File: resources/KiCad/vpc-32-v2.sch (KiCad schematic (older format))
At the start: 58 parts, among them CON1 Power jack, J1 SD_SOCKET, J2 PS/2, J3 video out, J4 RJ11, J5 audio out, K1 jumper, P1 gamepad 2, P2 ICSP, P3 gempad 1, Q1 2N3906, Q2 2N3904, SW1 reset, SW2 Power, U1 LM3940-3.3, U2 PIC32MX170F256B, U3 23LC1024, X1 10Mhz

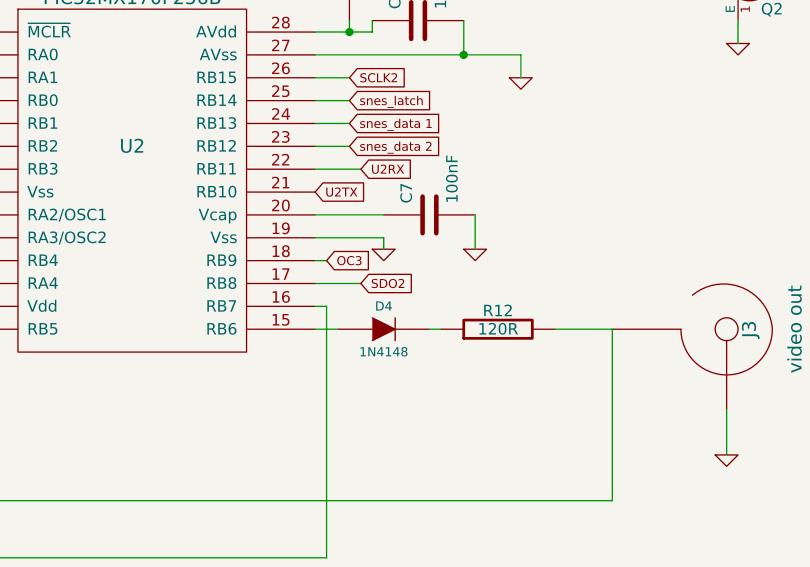
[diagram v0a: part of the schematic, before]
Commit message: ajout support sram et correction bug
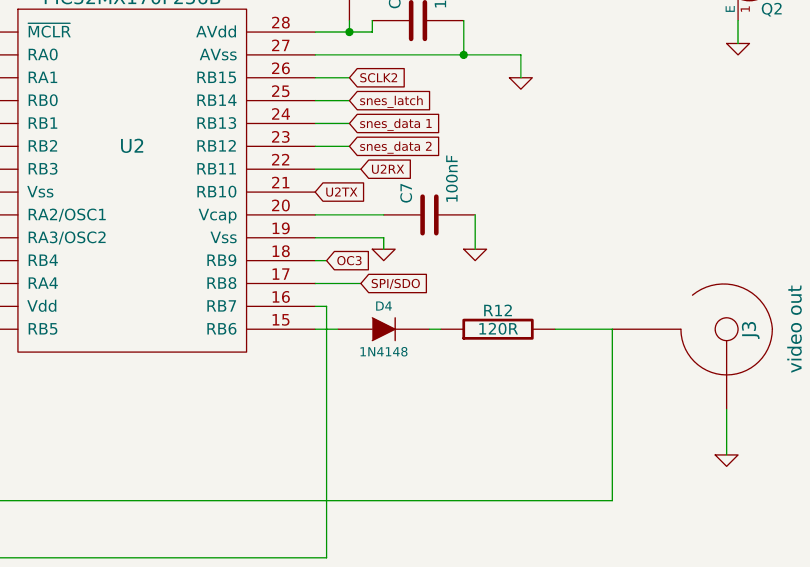
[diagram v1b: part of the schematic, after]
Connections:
- net SDO2 renamed SPI/SDO
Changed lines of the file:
@@
 Sheet 1 1
 Title ""
-Date "17 nov 2014"
+Date "24 nov 2014"
 Rev ""
 Comp ""
@@
 STATUS
 Text GLabel 6900 4150 2    39   Input ~ 0
-SDO2
+SPI/SDO
 Text GLabel 5000 3350 0    39   Input ~ 0
 PGED1/snes_clock

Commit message: travail sur vpcBASIC
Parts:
- added C14: 10µF, ~, symbol C
- added C15: 47µF, ~, symbol C
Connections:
- net +3,3V: now also C14.1, C15.1
- net GND: now also C14.2, C15.2
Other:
- note added: "+\n"
- note added: "C14 ceramic, SMD\nC1,C15 aluminum electrolytic through hole"
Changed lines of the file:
@@
 Sheet 1 1
 Title ""
-Date "24 nov 2014"
+Date "30 nov 2014"
 Rev ""
 Comp ""
@@
 $EndComp
 $Comp
-L GND #PWR21
+L GND #PWR23
 U 1 1 52181145
 P 8500 4900
-F 0 "#PWR21" H 8500 4900 30  0001 C CNN
+F 0 "#PWR23" H 8500 4900 30  0001 C CNN
 F 1 "GND" H 8500 4830 30  0001 C CNN
 F 2 "" H 8500 4900 60  0000 C CNN
@@
 +3,3V
 $Comp
-L GND #PWR16
+L GND #PWR18
 U 1 1 521812CB
 P 7000 4000
-F 0 "#PWR16" H 7000 4000 30  0001 C CNN
+F 0 "#PWR18" H 7000 4000 30  0001 C CNN
 F 1 "GND" H 7000 3930 30  0001 C CNN
 F 2 "" H 7000 4000 60  0000 C CNN
@@
 $EndComp
 $Comp
-L GND #PWR13
+L GND #PWR14
 U 1 1 521812EF
 P 4850 3750
-F 0 "#PWR13" H 4850 3750 30  0001 C CNN
+F 0 "#PWR14" H 4850 3750 30  0001 C CNN
 F 1 "GND" H 4850 3680 30  0001 C CNN
 F 2 "" H 4850 3750 60  0000 C CNN
@@
 $EndComp
 $Comp
-L GND #PWR17
+L GND #PWR19
 U 1 1 521A0F8C
 P 7400 4000
-F 0 "#PWR17" H 7400 4000 30  0001 C CNN
+F 0 "#PWR19" H 7400 4000 30  0001 C CNN
 F 1 "GND" H 7400 3930 30  0001 C CNN
 F 2 "" H 7400 4000 60  0000 C CNN
@@
 $EndComp
 $Comp
-L GND #PWR12
+L GND #PWR13
 U 1 1 521A10AE
 P 4600 2450
-F 0 "#PWR12" H 4600 2450 30  0001 C CNN
+F 0 "#PWR13" H 4600 2450 30  0001 C CNN
 F 1 "GND" H 4600 2380 30  0001 C CNN
 F 2 "" H 4600 2450 60  0000 C CNN
@@
 +3,3V
 $Comp
-L GND #PWR15
+L GND #PWR17
 U 1 1 521A28F4
 P 6000 1650
-F 0 "#PWR15" H 6000 1650 30  0001 C CNN
+F 0 "#PWR17" H 6000 1650 30  0001 C CNN
 F 1 "GND" H 6000 1580 30  0001 C CNN
 F 2 "" H 6000 1650 60  0000 C CNN
@@
 PGEC1
 $Comp
-L GND #PWR25
+L GND #PWR27
 U 1 1 521A78A1
 P 9750 2600
-F 0 "#PWR25" H 9750 2600 30  0001 C CNN
+F 0 "#PWR27" H 9750 2600 30  0001 C CNN
 F 1 "GND" H 9750 2530 30  0001 C CNN
 F 2 "" H 9750 2600 60  0000 C CNN
@@
 $EndComp
 $Comp
-L GND #PWR22
+L GND #PWR24
 U 1 1 521A7A94
 P 8550 3100
-F 0 "#PWR22" H 8550 3100 30  0001 C CNN
+F 0 "#PWR24" H 8550 3100 30  0001 C CNN
 F 1 "GND" H 8550 3030 30  0001 C CNN
 F 2 "" H 8550 3100 60  0000 C CNN
@@
 $EndComp
 $Comp
-L GND #PWR24
+L GND #PWR26
 U 1 1 521A7A9A
 P 9550 2950
-F 0 "#PWR24" H 9550 2950 30  0001 C CNN
+F 0 "#PWR26" H 9550 2950 30  0001 C CNN
 F 1 "GND" H 9550 2880 30  0001 C CNN
 F 2 "" H 9550 2950 60  0000 C CNN
@@
 $EndComp
 $Comp
-L GND #PWR19
+L GND #PWR21
 U 1 1 521A7BF6
 P 8150 2850
-F 0 "#PWR19" H 8150 2850 30  0001 C CNN
+F 0 "#PWR21" H 8150 2850 30  0001 C CNN
 F 1 "GND" H 8150 2780 30  0001 C CNN
 F 2 "" H 8150 2850 60  0000 C CNN
@@
 $EndComp
 $Comp
-L GND #PWR29
+L GND #PWR31
 U 1 1 521A9812
 P 10500 6350
-F 0 "#PWR29" H 10500 6350 30  0001 C CNN
+F 0 "#PWR31" H 10500 6350 30  0001 C CNN
 F 1 "GND" H 10500 6280 30  0001 C CNN
 F 2 "" H 10500 6350 60  0000 C CNN
@@
 $EndComp
 $Comp
-L GND #PWR26
+L GND #PWR28
 U 1 1 521A9A38
 P 9750 6450
-F 0 "#PWR26" H 9750 6450 30  0001 C CNN
+F 0 "#PWR28" H 9750 6450 30  0001 C CNN
 F 1 "GND" H 9750 6380 30  0001 C CNN
 F 2 "" H 9750 6450 60  0000 C CNN
@@
 $EndComp
 $Comp
-L GND #PWR23
+L GND #PWR25
 U 1 1 521A9A3E
 P 9250 6450
-F 0 "#PWR23" H 9250 6450 30  0001 C CNN
+F 0 "#PWR25" H 9250 6450 30  0001 C CNN
 F 1 "GND" H 9250 6380 30  0001 C CNN
 F 2 "" H 9250 6450 60  0000 C CNN
@@
 $EndComp
 $Comp
-L GND #PWR20
+L GND #PWR22
 U 1 1 521A9A4E
 P 8450 6450
-F 0 "#PWR20" H 8450 6450 30  0001 C CNN
+F 0 "#PWR22" H 8450 6450 30  0001 C CNN
 F 1 "GND" H 8450 6380 30  0001 C CNN
 F 2 "" H 8450 6450 60  0000 C CNN
@@
 $EndComp
 $Comp
-L GND #PWR14
+L GND #PWR16
 U 1 1 521E10D5
 P 5600 7200
-F 0 "#PWR14" H 5600 7200 30  0001 C CNN
+F 0 "#PWR16" H 5600 7200 30  0001 C CNN
 F 1 "GND" H 5600 7130 30  0001 C CNN
 F 2 "" H 5600 7200 60  0000 C CNN
@@
 PGEC1/~CS1
 $Comp
-L GND #PWR18
+L GND #PWR20
 U 1 1 5225165F
 P 7600 3250
-F 0 "#PWR18" H 7600 3250 30  0001 C CNN
+F 0 "#PWR20" H 7600 3250 30  0001 C CNN
 F 1 "GND" H 7600 3180 30  0001 C CNN
 F 2 "" H 7600 3250 60  0000 C CNN
@@
 $EndComp
 $Comp
-L GND #PWR28
+L GND #PWR30
 U 1 1 538B65CC
 P 10150 4900
-F 0 "#PWR28" H 10150 4900 30  0001 C CNN
+F 0 "#PWR30" H 10150 4900 30  0001 C CNN
 F 1 "GND" H 10150 4830 30  0001 C CNN
 F 2 "" H 10150 4900 60  0000 C CNN
@@
 $EndComp
 $Comp
-L GND #PWR27
+L GND #PWR29
 U 1 1 538B65D2
 P 10150 4000
-F 0 "#PWR27" H 10150 4000 30  0001 C CNN
+F 0 "#PWR29" H 10150 4000 30  0001 C CNN
 F 1 "GND" H 10150 3930 30  0001 C CNN
 F 2 "" H 10150 4000 60  0000 C CNN
@@
 Connection ~ 2900 5750
 Connection ~ 1650 6050
+$Comp
+L C C15
+U 1 1 547B4E3E
+P 4850 6900
+F 0 "C15" H 4850 7000 40  0000 L CNN
+F 1 "47µF" H 4856 6815 40  0000 L CNN
+F 2 "~" H 4888 6750 30  0000 C CNN
+F 3 "~" H 4850 6900 60  0000 C CNN
+	1    4850 6900
+	1    0    0    -1
+$EndComp
+$Comp
+L C C14
+U 1 1 547B4E4B
+P 4450 6900
+F 0 "C14" H 4450 7000 40  0000 L CNN
+F 1 "10µF" H 4456 6815 40  0000 L CNN
+F 2 "~" H 4488 6750 30  0000 C CNN
+F 3 "~" H 4450 6900 60  0000 C CNN
+	1    4450 6900
+	1    0    0    -1
+$EndComp
+$Comp
+L GND #PWR15
+U 1 1 547B4E51
+P 4850 7200
+F 0 "#PWR15" H 4850 7200 30  0001 C CNN
+F 1 "GND" H 4850 7130 30  0001 C CNN
+F 2 "" H 4850 7200 60  0000 C CNN
+F 3 "" H 4850 7200 60  0000 C CNN
+	1    4850 7200
+	1    0    0    -1
+$EndComp
+$Comp
+L GND #PWR12
+U 1 1 547B4E57
+P 4450 7200
+F 0 "#PWR12" H 4450 7200 30  0001 C CNN
+F 1 "GND" H 4450 7130 30  0001 C CNN
+F 2 "" H 4450 7200 60  0000 C CNN
+F 3 "" H 4450 7200 60  0000 C CNN
+	1    4450 7200
+	1    0    0    -1
+$EndComp
+Wire Wire Line
+	4450 7100 4450 7200
+Wire Wire Line
+	4850 7100 4850 7200
+Wire Wire Line
+	4450 6700 4450 6750
+Connection ~ 4450 6700
+Text Notes 4750 6850 0    60   ~ 0
++\n
+Text Notes 4150 7450 0    60   ~ 0
+C14 ceramic, SMD\nC1,C15 aluminum electrolytic through hole
 $EndSCHEMATC
